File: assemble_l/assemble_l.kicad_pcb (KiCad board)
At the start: 2 copper layers, 128.5 x 92.1 mm, 45 parts, among them J1 Conn_01x02_Pin, SW1 SW_Push, SW10 SW_Push, SW11 SW_Push, SW12 SW_Push, SW13 SW_Push, SW14 SW_Push, SW15 SW_Push, SW16 SW_Push, SW17 SW_Push, SW18 SW_Push, SW19 SW_Push, SW2 SW_Push, SW20 SW_Push, SW21 SW_Push, SW22 SW_Push, SW3 SW_Push, SW4 SW_Push, SW5 SW_Push, SW6 SW_Push, SW7 SW_Push, SW8 SW_Push, SW9 SW_Push, U1 Micon_BLEMicroPro

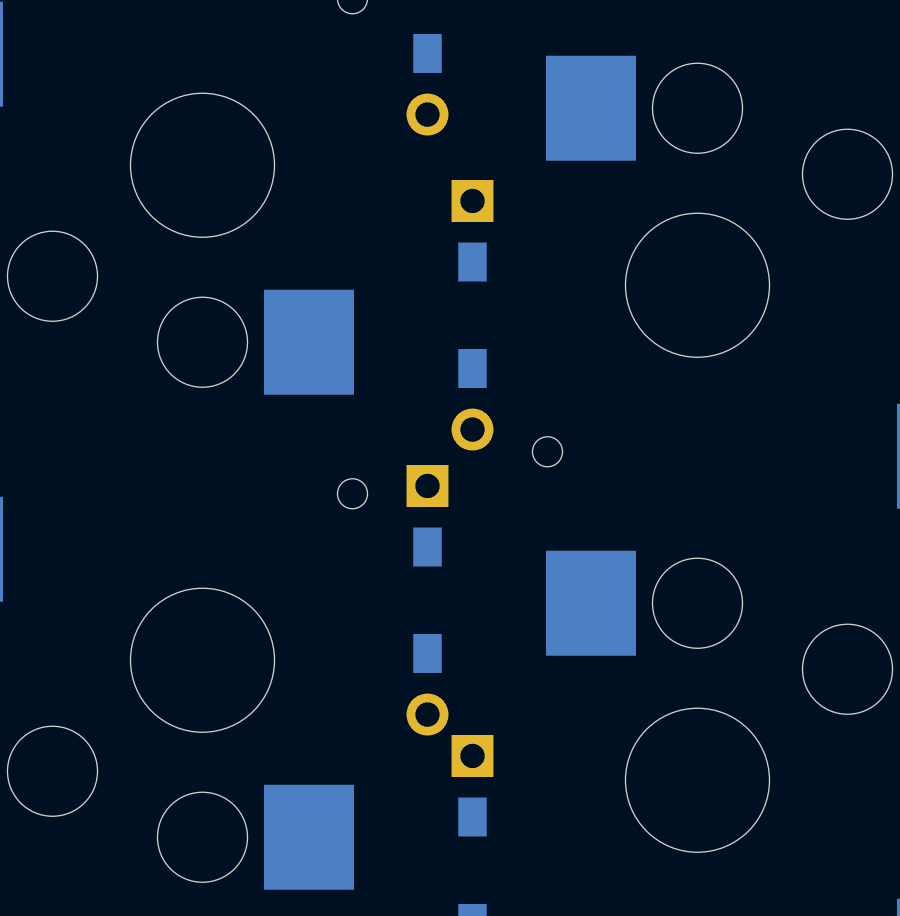
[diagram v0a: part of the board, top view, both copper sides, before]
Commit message: fix: some diode place
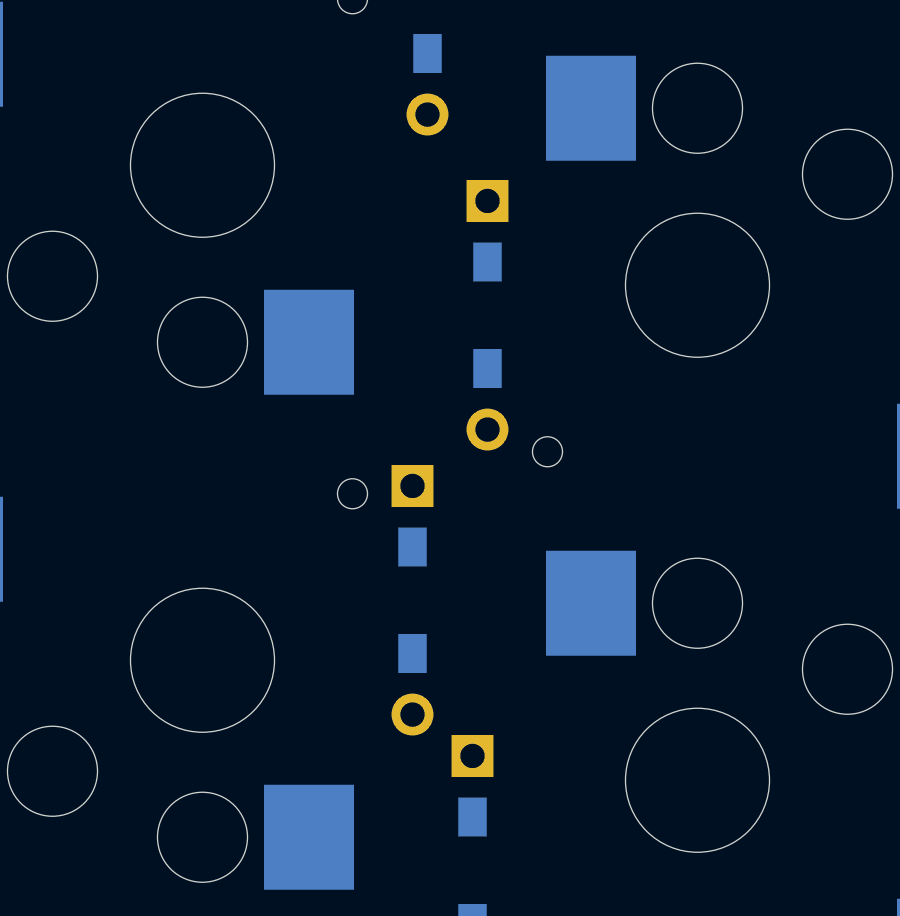
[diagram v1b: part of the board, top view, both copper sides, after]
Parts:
- moved D11 0.50 mm to (124.5, 54.0)
- moved D14 0.50 mm to (127.0, 44.5)
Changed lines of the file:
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@@
 		)
 		(fp_line
-			(start -1.999998 7.43)
+			(start -1.999997 7.43)
 			(end -2 3.4)
 			(stroke
@@
 		)
 		(fp_line
-			(start 1.7 7.820002)
+			(start 1.7 7.820003)
 			(end 1.7 3.99)
 			(stroke
@@
 	(footprint "kbd_Parts:Diode_TH_SMD"
 		(layer "F.Cu")
-		(at 125 54 -90)
+		(at 124.5 54 -90)
 		(descr "Resitance 3 pas")
 		(tags "R")
@@
 	(footprint "kbd_Parts:Diode_TH_SMD"
 		(layer "F.Cu")
-		(at 126.5 44.5 -90)
+		(at 127 44.5 -90)
 		(descr "Resitance 3 pas")
 		(tags "R")

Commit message: fix: re-change layout
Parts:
- moved D3 46.3 mm to (61.5, 81.0), turned to 90 degrees
- moved SW3 36.9 mm to (68.0, 80.5), turned to 180 degrees
- moved D8 19.6 mm to (108.5, 69.0)
- moved D4 19.2 mm to (92.0, 50.8)
- moved SW9 18.6 mm to (84.5, 80.5)
- moved D5 17.6 mm to (92.0, 67.3)
- moved D9 17.1 mm to (91.5, 83.5)
- moved D16 17.0 mm to (141.5, 73.5)
- moved SW4 16.5 mm to (84.5, 47.5)
- moved SW5 16.5 mm to (84.5, 64.0)
- moved D7 16.4 mm to (108.5, 52.5)
- moved D15 16.2 mm to (141.5, 57.0)
- moved D10 15.1 mm to (110.0, 36.0)
- moved D14 15.0 mm to (141.5, 40.5)
- moved D13 6.50 mm to (121.5, 99.0)
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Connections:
- D3 pad 1: Row0 -> Row2
- D4 pad 1: Row1 -> Row0
- D5 pad 1: Row2 -> Row1
- D6 pad 1: Row0 -> Row2
- D7 pad 1: Row1 -> Row0
- D8 pad 1: Row2 -> Row1
- D9 pad 1: Row3 -> Row2
- SW3 pad 1: Col1 -> Col0
- SW6 pad 1: Col2 -> Col1
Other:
- outline, holes or cut-outs redrawn

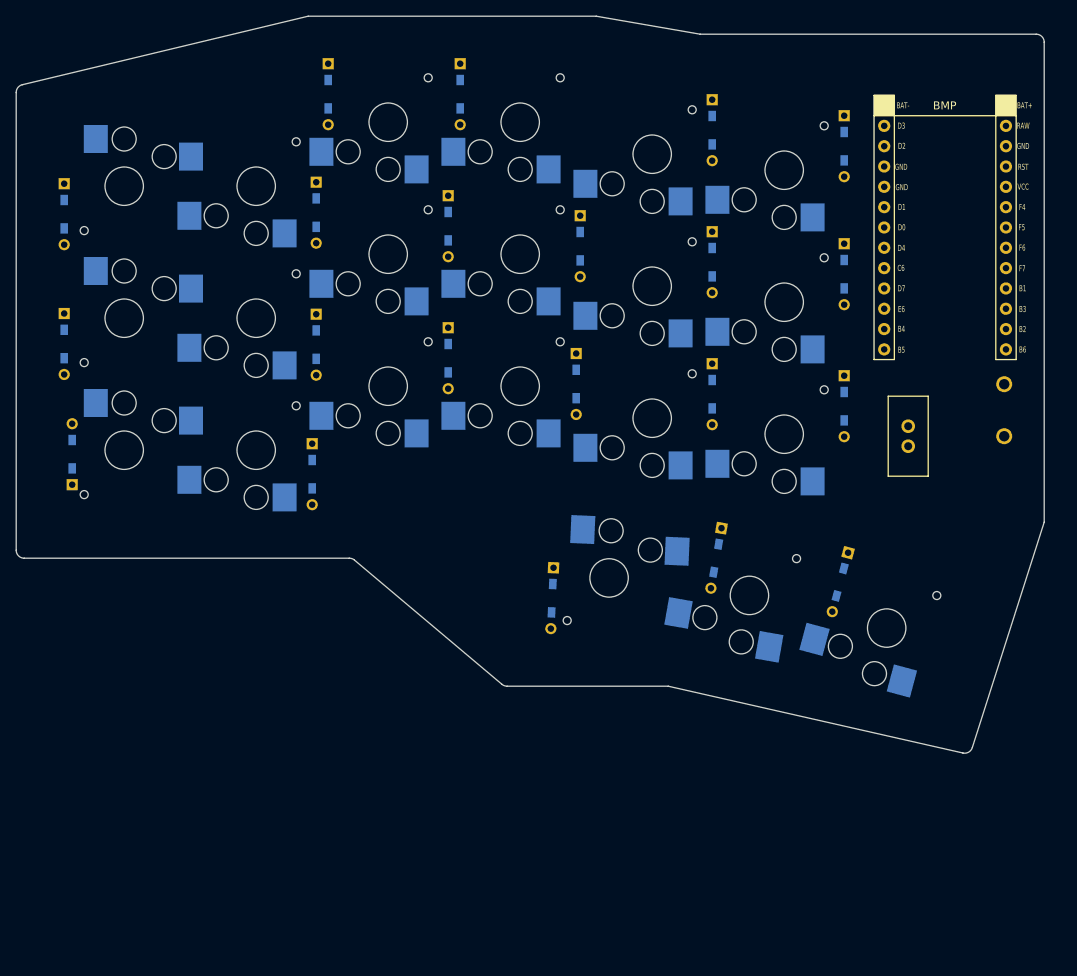
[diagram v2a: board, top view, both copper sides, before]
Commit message: fix: change outline
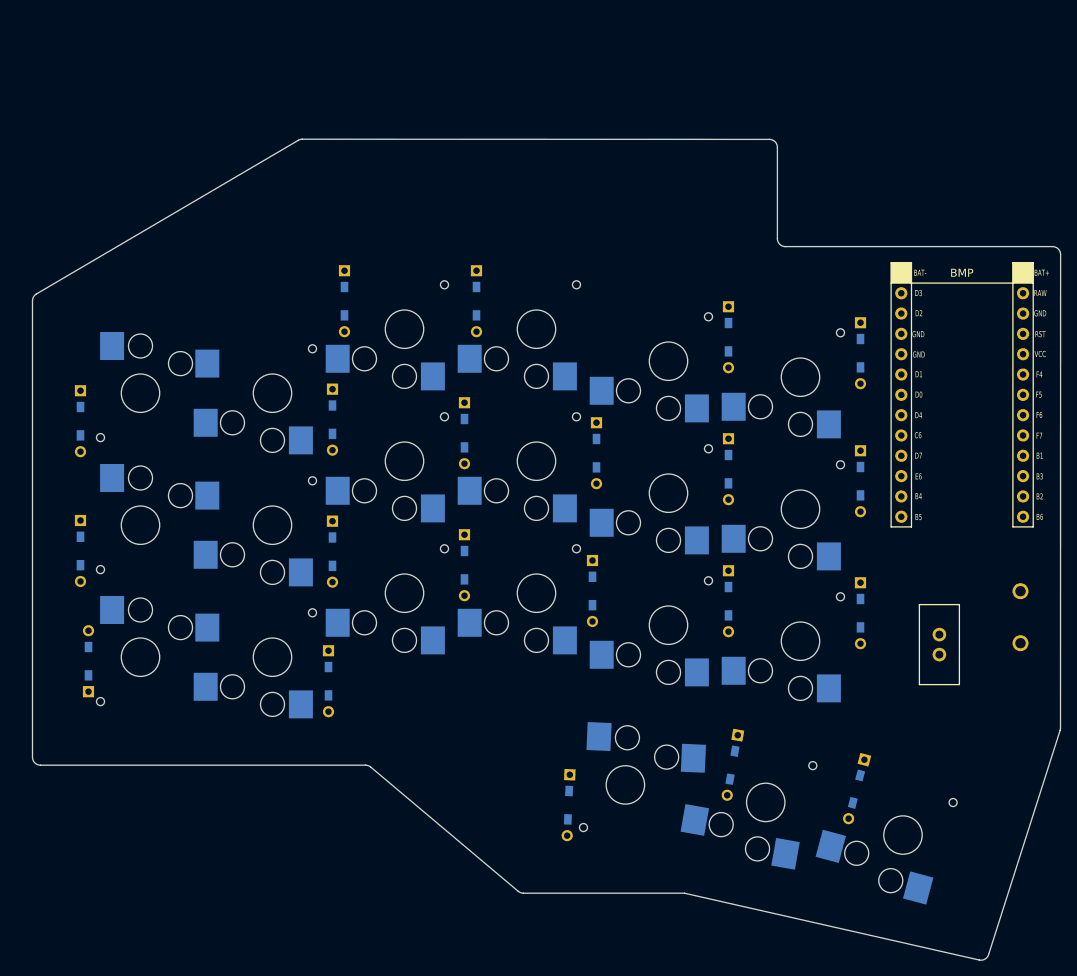
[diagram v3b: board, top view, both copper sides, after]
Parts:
- moved J1 26.3 mm to (169.9, 104.8)
- moved SW21 26.0 mm to (165.3, 128.6)
- moved D1 26.0 mm to (62.5, 76.9)
- moved D10 26.0 mm to (112.0, 61.9)
- moved D11 26.0 mm to (127.0, 80.9)
- moved D12 26.0 mm to (126.5, 98.1)
- moved D13 26.0 mm to (123.5, 124.9)
- moved D14 26.0 mm to (143.5, 66.4)
- moved D15 26.0 mm to (143.5, 82.9)
- moved D16 26.0 mm to (143.5, 99.4)
- moved D17 26.0 mm to (144.0, 119.9)
- moved D18 26.0 mm to (160.0, 68.4)
- moved D19 26.0 mm to (160.0, 84.4)
- moved D2 26.0 mm to (62.5, 93.1)
- moved D20 26.0 mm to (160.0, 100.9)
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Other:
- board size 128.5 x 92.1 mm -> 128.5 x 102.6 mm

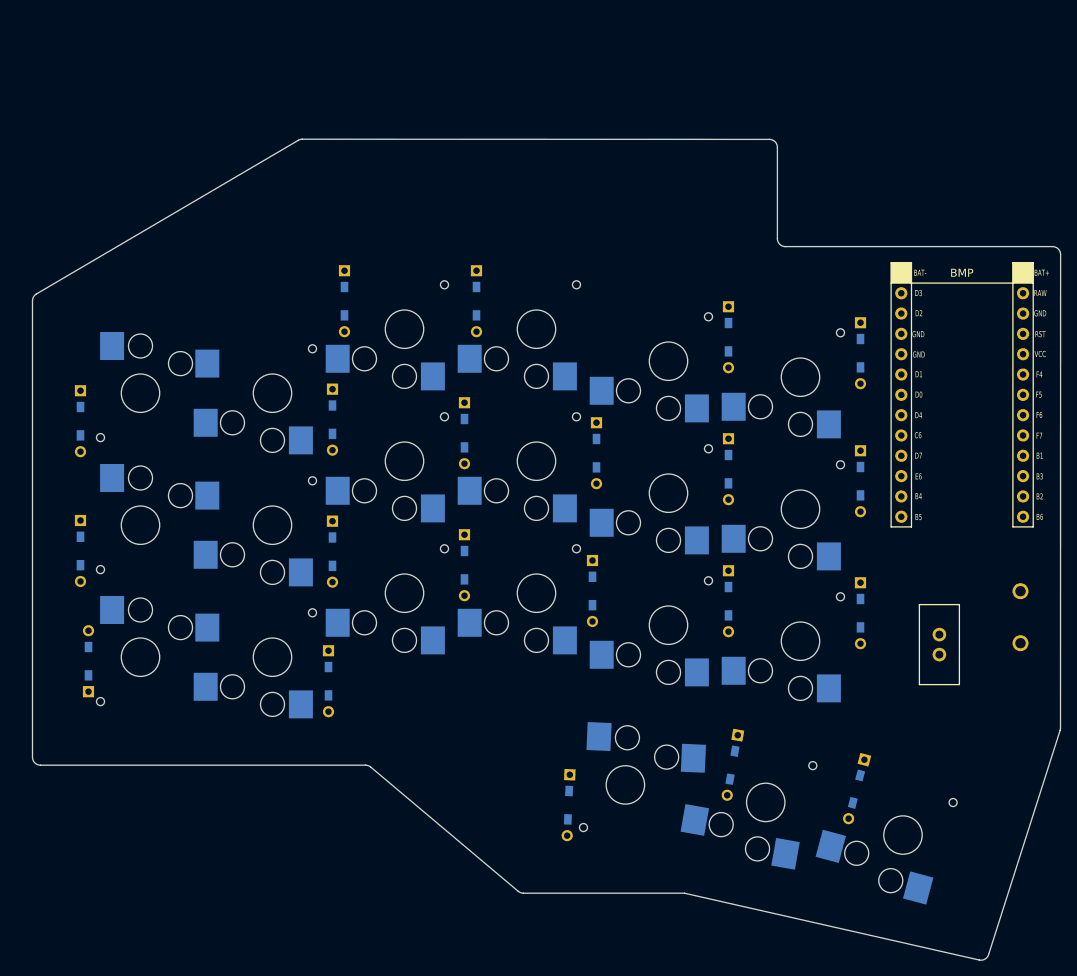
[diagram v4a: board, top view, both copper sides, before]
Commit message: feat: add screw
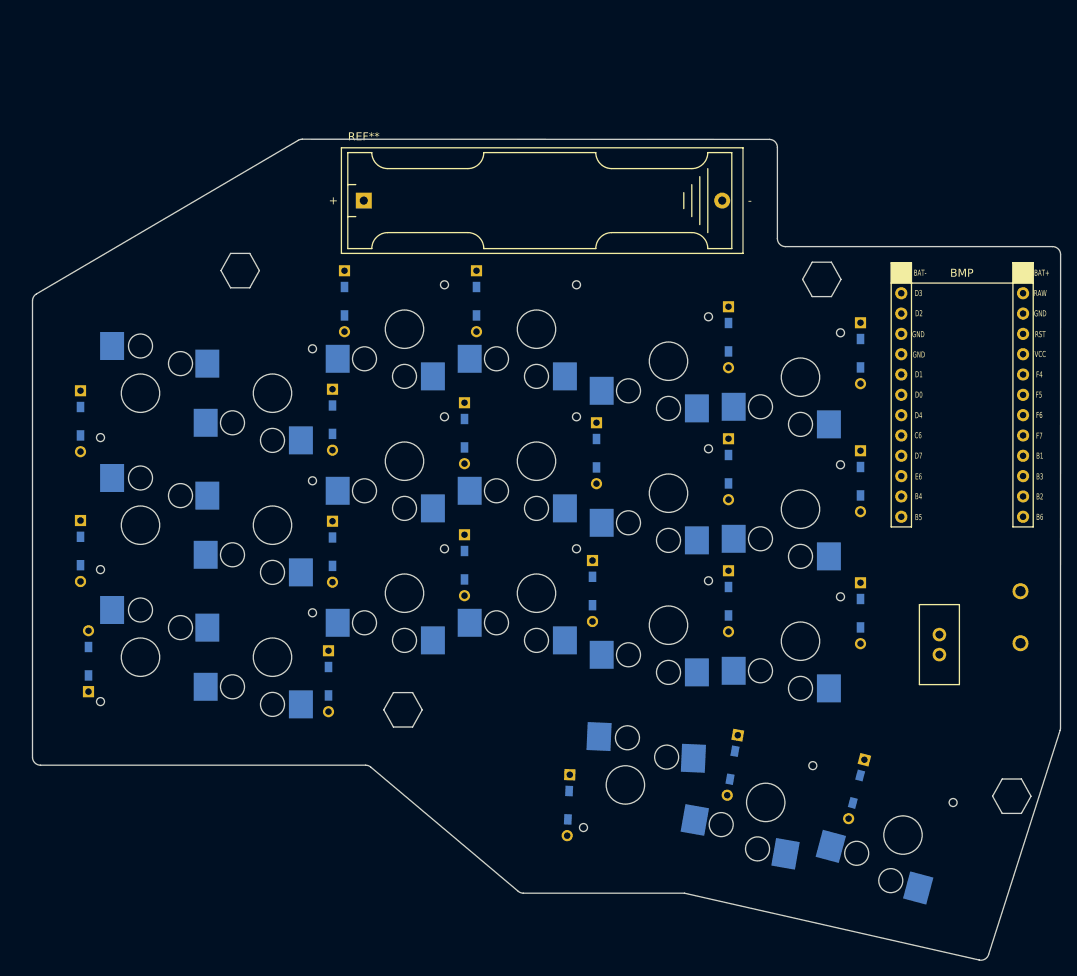
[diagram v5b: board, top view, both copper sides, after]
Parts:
- added REF**: BatteryHolder_単4, kbd_Parts:Battery_AAA, F.Cu at (98.0, 49.3)
- added Ref**: Val**, kbd_Hole:m2_Spacer_Hole_hex, F.Cu at (155.2, 59.1)
- added Ref**: Val**, kbd_Hole:m2_Spacer_Hole_hex, F.Cu at (102.8, 113.0)
- added Ref**: Val**, kbd_Hole:m2_Spacer_Hole_hex, F.Cu at (82.5, 58.0)
- added Ref**: Val**, kbd_Hole:m2_Spacer_Hole_hex, F.Cu at (178.9, 123.8)

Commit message: feat: update PCB
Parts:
- removed J1: Conn_01x02_Pin, kbd_Parts:Battery_2pin
- removed REF**: BatteryHolder_単4, kbd_Parts:Battery_AAA
- added AE-XCL: Regulator, kicad-lib:AE-XCL102D333CR-G, F.Cu at (169.0, 103.5)
- added BT1: Battery_Cell, kbd_Parts:Battery_AAA, F.Cu at (98.0, 49.3)
- added SW23: SW_SPDT, kbd_Parts:TGSW_MSK-12D19, F.Cu at (180.7, 107.5)
- moved SW22 3.24 mm to (180.3, 98.2)
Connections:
- U1 pad 26: GND -> Bat-

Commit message: feat: wiring in left
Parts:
- D1, D10, D11, D12, D13, D14, D15, D16, D17, D18, D19, D2, D20, D21, D3, D4, D5, D6, D7, D8, D9: footprint kbd_Parts:Diode_TH_SMD -> kbd_Parts:Diode_SMD
- moved D6 48.1 mm to (94.8, 110.0)
- moved SW6 44.2 mm to (86.5, 106.4)
- moved D8 18.8 mm to (94.8, 84.8)
- moved D7 18.5 mm to (94.8, 68.6)
- moved SW9 18.2 mm to (103.0, 98.5), turned to 180 degrees
- moved SW7 16.4 mm to (103.0, 65.5), turned to 180 degrees
- moved SW8 16.4 mm to (103.0, 82.0), turned to 180 degrees
- moved D10 15.1 mm to (127.0, 64.0)
- moved D21 14.7 mm to (173.2, 128.2)
- moved D17 12.4 mm to (156.2, 122.0)
- moved D9 7.23 mm to (94.8, 102.2)
- moved D3 2.82 mm to (62.5, 109.5), turned to -90 degrees
- moved D20 2.38 mm to (160.0, 103.2)
- moved D16 1.38 mm to (143.5, 100.8)
- moved D1 0.88 mm to (62.5, 76.0)
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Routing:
- net Col0: track 0.00 -> 172.5 mm, vias 0 -> 5
- net Col3: track 0.00 -> 170.7 mm, vias 0 -> 7
- net Col1: track 0.00 -> 166.9 mm, vias 0 -> 6
- net Row2: track 0.00 -> 158.7 mm, vias 0 -> 1
- net Col4: track 0.00 -> 150.6 mm, vias 0 -> 10
- net Row0: track 0.00 -> 148.4 mm, vias 0 -> 1
- net Col2: track 0.00 -> 145.8 mm, vias 0 -> 5
- net Row1: track 0.00 -> 139.6 mm, vias 0 -> 1
- net Col5: track 0.00 -> 133.1 mm, vias 0 -> 6
- net Net-(BT1-+): track 0.00 -> 117.5 mm
- net Row3: track 0.00 -> 112.3 mm, vias 0 -> 1
- net Bat-: track 0.00 -> 84.9 mm, vias 0 -> 2
- net Bat+: track 0.00 -> 61.3 mm
- net GND: track 0.00 -> 56.9 mm, vias 0 -> 3
- net Reset: track 0.00 -> 39.3 mm, vias 0 -> 1
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
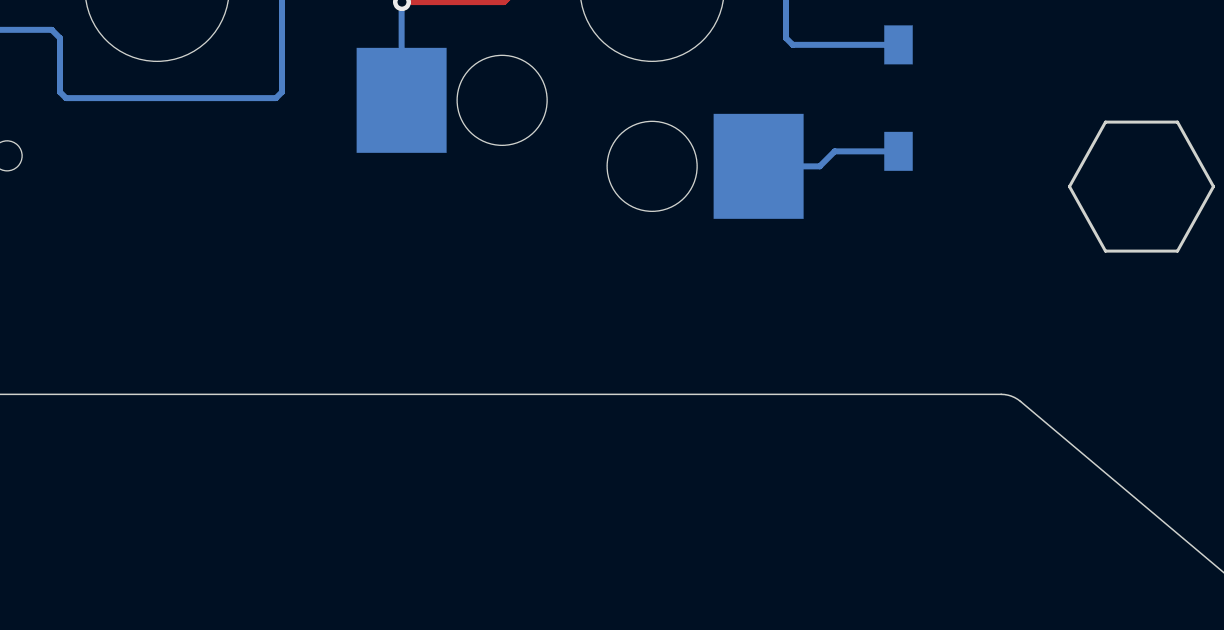
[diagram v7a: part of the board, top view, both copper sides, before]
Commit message: feat: add signature and version
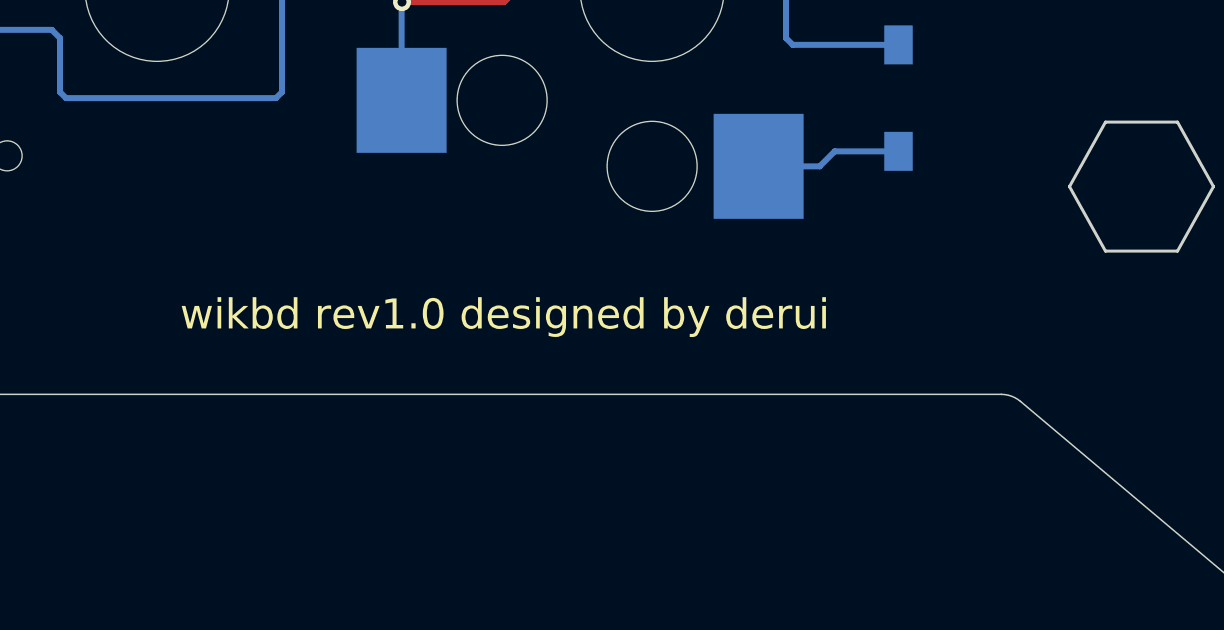
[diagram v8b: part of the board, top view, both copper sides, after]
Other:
- board text added: "wikbd rev1.0 designed by derui"
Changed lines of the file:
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@@
 		(fp_line
 			(start -5.65 6)
-			(end -5.65 1.400001)
+			(end -5.65 1.400002)
 			(stroke
 				(width 0.15)
@@
 		(fp_line
 			(start -4.6 6)
-			(end -4.599999 1.4)
+			(end -4.599998 1.4)
 			(stroke
 				(width 0.15)
@@
 		(fp_line
 			(start 1.3 3.575001)
-			(end -1.275 3.575001)
+			(end -1.275 3.575002)
 			(stroke
 				(width 0.15)
@@
 		)
 		(fp_arc
-			(start -1.275 3.575001)
+			(start -1.275 3.575002)
 			(mid -2.10585 3.23085)
 			(end -2.45 2.4)
@@
 		)
 		(fp_line
-			(start -0.549999 8.2)
+			(start -0.549998 8.2)
 			(end -0.55 3.6)
 			(stroke
@@
 		)
 		(fp_line
-			(start -1.999999 7.43)
+			(start -1.999998 7.43)
 			(end -2 3.4)
 			(stroke
@@
 		)
 		(fp_line
-			(start -2.299999 7.2)
+			(start -2.299998 7.2)
 			(end -1.025 8.225)
 			(stroke
@@
 		)
 		(fp_line
-			(start -2.299999 7.2)
+			(start -2.299998 7.2)
 			(end -2.3 3.05)
 			(stroke
@@
 		(fp_line
 			(start -3.25 6.25)
-			(end -3.25 1.400001)
+			(end -3.25 1.400002)
 			(stroke
 				(width 0.15)
@@
 			(start -4.3 6.017458)
 			(mid -3.138277 6.335211)
-			(end -2.299999 7.2)
+			(end -2.299998 7.2)
 			(stroke
 				(width 0.15)
@@
 		(fp_arc
 			(start -7.305 2.375)
-			(mid -7.012106 1.667893)
+			(mid -7.012105 1.667893)
 			(end -6.305 1.375)
 			(stroke
@@
 		)
 		(fp_line
-			(start -6.250001 6)
+			(start -6.250002 6)
 			(end -6.25 1.4)
 			(stroke
@@
 		(fp_line
 			(start -1.3 7.99)
-			(end -1.300001 3.6)
+			(end -1.300002 3.6)
 			(stroke
 				(width 0.15)
@@
 		)
 		(fp_line
-			(start 1.7 7.820001)
+			(start 1.7 7.820002)
 			(end 1.7 3.99)
 			(stroke
@@
 		)
 		(fp_line
-			(start 1.85 7.660001)
+			(start 1.85 7.660002)
 			(end 1.85 4.13)
 			(stroke
@@
 		(layer "Edge.Cuts")
 	)
+	(gr_text "wikbd rev1.0 designed by derui\n"
+		(at 70.8 117.8 0)
+		(layer "F.SilkS")
+		(effects
+			(font
+				(size 1 1)
+				(thickness 0.1)
+			)
+			(justify left bottom)
+		)
+	)
 	(segment
